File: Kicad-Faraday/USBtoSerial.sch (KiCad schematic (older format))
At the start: 10 parts, among them P16 USB-MICRO-B, U10 NUF2101MT1G, U6 FT230XQ-R

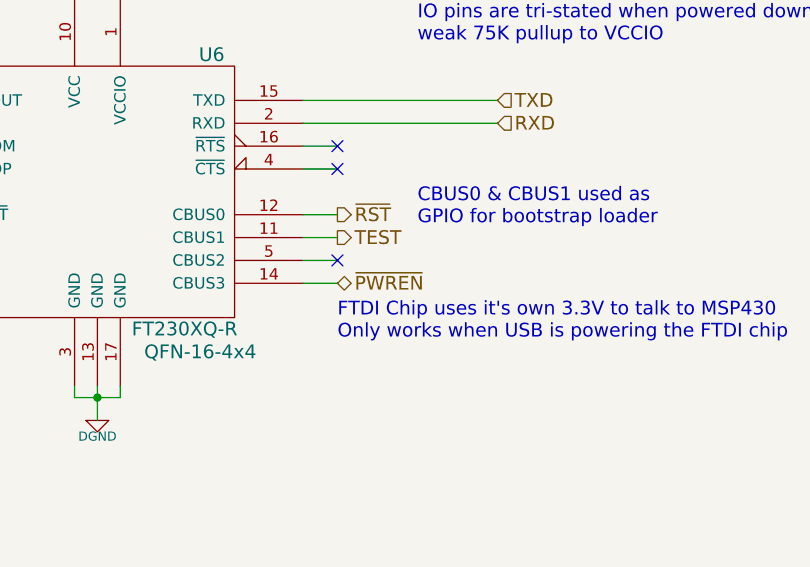
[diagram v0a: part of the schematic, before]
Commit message: Updated per RevD Github Issue comments. Largely removed unnecessary items
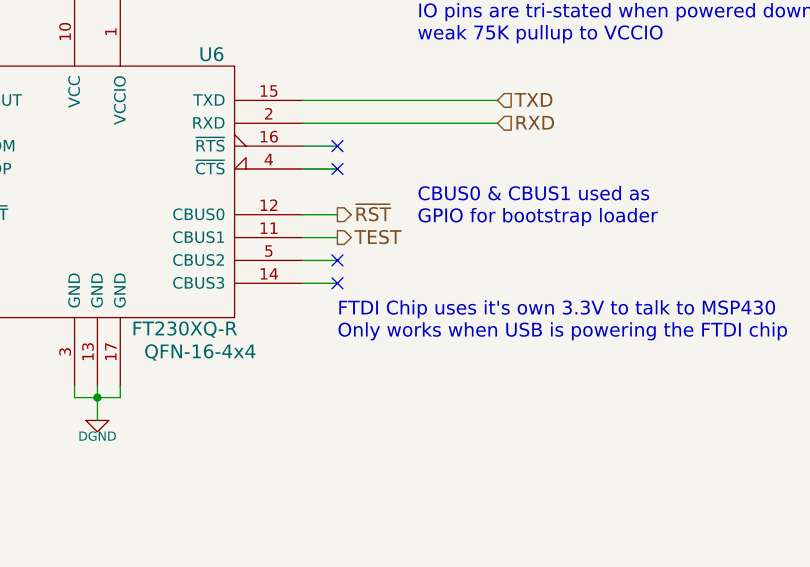
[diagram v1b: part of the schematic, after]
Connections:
- net ~PWREN~: no longer names the net of U6.14 (CBUS3)
- no-connect marks 4 -> 5
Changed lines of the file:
@@
 Sheet 8 11
 Title "Faraday Wireless Node"
-Date "24 oct 2016"
+Date "10 nov 2016"
 Rev "C"
 Comp "FaradayRF"
@@
 $EndComp
 $Comp
-L PWR_FLAG #FLG078
+L PWR_FLAG #FLG072
 U 1 1 54090954
 P 800 6000
-F 0 "#FLG078" H 800 6095 30  0001 C CNN
+F 0 "#FLG072" H 800 6095 30  0001 C CNN
 F 1 "PWR_FLAG" H 800 6180 30  0000 C CNN
 F 2 "" H 800 6000 60  0000 C CNN
@@
 5V USB
 $Comp
-L PWR_FLAG #FLG079
+L PWR_FLAG #FLG073
 U 1 1 54170CB7
 P 7000 4550
-F 0 "#FLG079" H 7000 4645 30  0001 C CNN
+F 0 "#FLG073" H 7000 4645 30  0001 C CNN
 F 1 "PWR_FLAG" H 7000 4730 30  0000 C CNN
 F 2 "" H 7000 4550 60  0000 C CNN
@@
 FTDI 3.3V OUT\nPower Flag
 $Comp
-L PWR_FLAG #FLG080
+L PWR_FLAG #FLG074
 U 1 1 541715EA
 P 5250 2650
-F 0 "#FLG080" H 5250 2745 30  0001 C CNN
+F 0 "#FLG074" H 5250 2745 30  0001 C CNN
 F 1 "PWR_FLAG" H 5250 2830 30  0000 C CNN
 F 2 "" H 5250 2650 60  0000 C CNN
@@
 $EndComp
 $Comp
-L DGND #PWR081
+L DGND #PWR075
 U 1 1 55A55E2C
 P 8350 6000
-F 0 "#PWR081" H 8350 6000 40  0001 C CNN
+F 0 "#PWR075" H 8350 6000 40  0001 C CNN
 F 1 "DGND" H 8350 5930 40  0000 C CNN
 F 2 "~" H 8350 6000 60  0000 C CNN
@@
 $EndComp
 $Comp
-L DGND #PWR082
+L DGND #PWR076
 U 1 1 55A55E8C
 P 7000 4250
-F 0 "#PWR082" H 7000 4250 40  0001 C CNN
+F 0 "#PWR076" H 7000 4250 40  0001 C CNN
 F 1 "DGND" H 7000 4180 40  0000 C CNN
 F 2 "~" H 7000 4250 60  0000 C CNN
@@
 $EndComp
 $Comp
-L DGND #PWR083
+L DGND #PWR077
 U 1 1 55A55E92
 P 7600 3300
-F 0 "#PWR083" H 7600 3300 40  0001 C CNN
+F 0 "#PWR077" H 7600 3300 40  0001 C CNN
 F 1 "DGND" H 7600 3230 40  0000 C CNN
 F 2 "~" H 7600 3300 60  0000 C CNN
@@
 $EndComp
 $Comp
-L DGND #PWR084
+L DGND #PWR078
 U 1 1 55A55E9E
 P 2100 6900
-F 0 "#PWR084" H 2100 6900 40  0001 C CNN
+F 0 "#PWR078" H 2100 6900 40  0001 C CNN
 F 1 "DGND" H 2100 6830 40  0000 C CNN
 F 2 "~" H 2100 6900 60  0000 C CNN
@@
 $EndComp
 $Comp
-L DGND #PWR085
+L DGND #PWR079
 U 1 1 55A55EA4
 P 1550 6900
-F 0 "#PWR085" H 1550 6900 40  0001 C CNN
+F 0 "#PWR079" H 1550 6900 40  0001 C CNN
 F 1 "DGND" H 1550 6830 40  0000 C CNN
 F 2 "~" H 1550 6900 60  0000 C CNN
@@
 $EndComp
 $Comp
-L +5V #PWR086
+L +5V #PWR080
 U 1 1 5788A803
 P 8250 2700
-F 0 "#PWR086" H 8250 2790 20  0001 C CNN
+F 0 "#PWR080" H 8250 2790 20  0001 C CNN
 F 1 "+5V" H 8250 2790 30  0000 C CNN
 F 2 "" H 8250 2700 60  0000 C CNN
@@
 	1    0    0    -1
 $EndComp
-Text HLabel 9400 5400 2    60   3State ~ 0
-~PWREN~
 $Comp
 L C C41
@@
 $EndComp
 $Comp
-L DGND #PWR087
+L DGND #PWR081
 U 1 1 578BD7EF
 P 5550 3300
-F 0 "#PWR087" H 5550 3300 40  0001 C CNN
+F 0 "#PWR081" H 5550 3300 40  0001 C CNN
 F 1 "DGND" H 5550 3230 40  0000 C CNN
 F 2 "~" H 5550 3300 60  0000 C CNN
@@
 $EndComp
 $Comp
-L DGND #PWR088
+L DGND #PWR082
 U 1 1 578CED94
 P 1100 6900
-F 0 "#PWR088" H 1100 6900 40  0001 C CNN
+F 0 "#PWR082" H 1100 6900 40  0001 C CNN
 F 1 "DGND" H 1100 6830 40  0000 C CNN
 F 2 "~" H 1100 6900 60  0000 C CNN
@@
 $EndComp
 $Comp
-L GNDPWR #PWR089
+L GNDPWR #PWR083
 U 1 1 578D0220
 P 800 6900
-F 0 "#PWR089" H 800 6950 40  0001 C CNN
+F 0 "#PWR083" H 800 6950 40  0001 C CNN
 F 1 "GNDPWR" H 800 6820 40  0000 C CNN
 F 2 "" H 800 6900 60  0000 C CNN
@@
 1Meg resistor for shield dischard\n4.7nF capacitor for RF noise
 $Comp
-L PWR_FLAG #FLG090
+L PWR_FLAG #FLG084
 U 1 1 578DEE25
 P 2300 6000
-F 0 "#FLG090" H 2300 6095 30  0001 C CNN
+F 0 "#FLG084" H 2300 6095 30  0001 C CNN
 F 1 "PWR_FLAG" H 2300 6180 30  0000 C CNN
 F 2 "" H 2300 6000 60  0000 C CNN
@@
 Wire Wire Line
 	9250 5300 9400 5300
-Wire Wire Line
-	9250 5400 9400 5400
 Wire Wire Line
 	5250 2650 5250 2700
@@
 IO pins are tri-stated when powered down,\nweak 75K pullup to VCCIO
 NoConn ~ 1950 5000
+NoConn ~ 9400 5400
+Wire Wire Line
+	9250 5400 9400 5400
 $EndSCHEMATC

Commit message: Adding Rev D files for night
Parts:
- C40: value 0.01uF -> 0.1uF
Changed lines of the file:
@@
 Sheet 8 11
 Title "Faraday Wireless Node"
-Date "13 nov 2016"
+Date "14 nov 2016"
 Rev "C"
 Comp "FaradayRF"
@@
 P 1100 6550
 F 0 "C40" H 1200 6600 50  0000 L CNN
-F 1 "0.01uF" H 1200 6525 50  0000 L CNN
+F 1 "0.1uF" H 1200 6525 50  0000 L CNN
 F 2 "C0402" H 1325 6375 50  0000 C CNN
 F 3 "" H 1100 6550 60  0000 C CNN

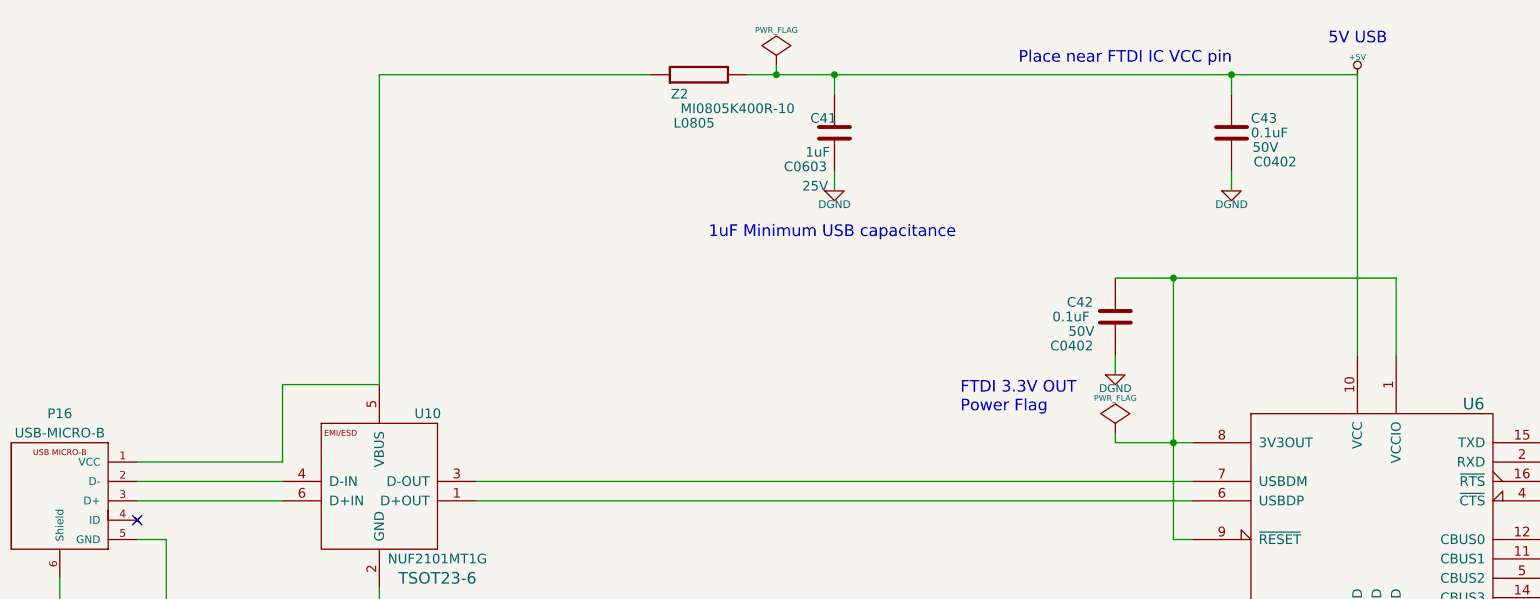
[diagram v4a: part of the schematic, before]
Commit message: Cleaned up a few connections on the schematic to make sure wire junctions were used. Also added a few notes such as LED color. Output new PDF of Schematics and updated Rev to Rev D1 for PCB:NG
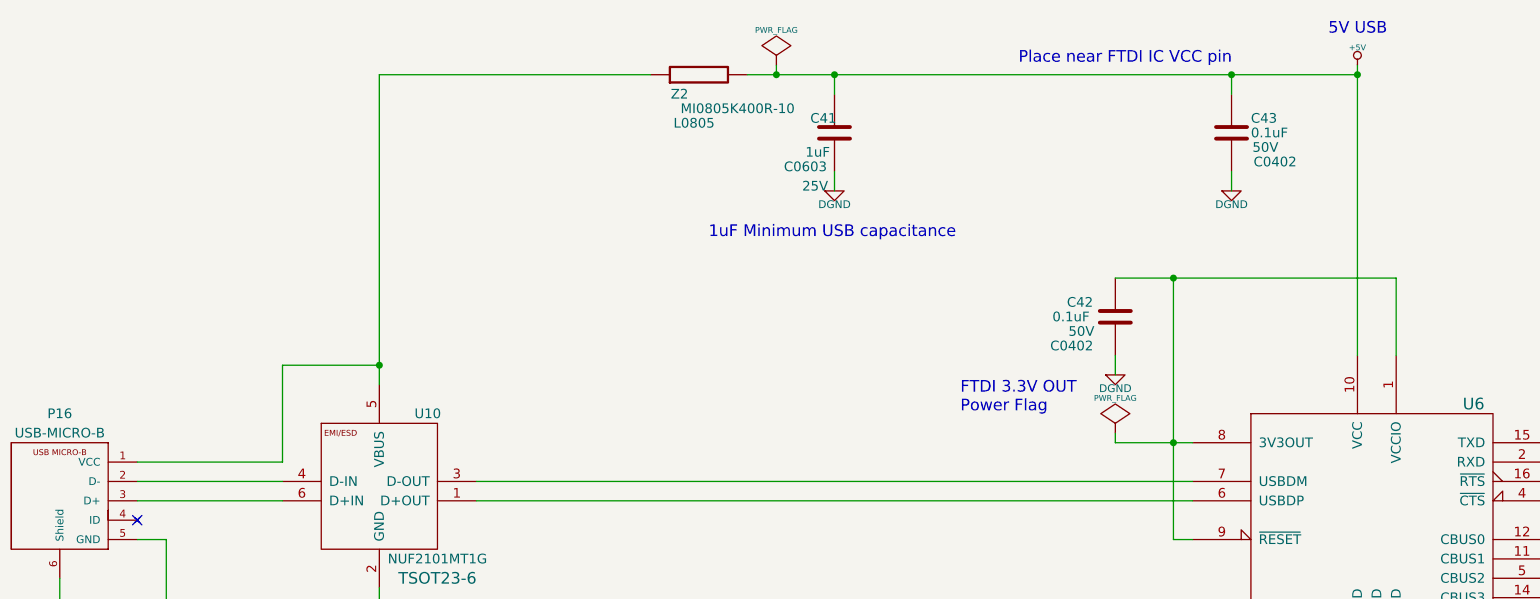
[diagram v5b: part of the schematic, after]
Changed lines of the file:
@@
 Sheet 8 11
 Title "Faraday Wireless Node"
-Date "14 nov 2016"
-Rev "C"
+Date "15 nov 2016"
+Rev "D1"
 Comp "FaradayRF"
 Comment1 "www.FaradayRF.com"
@@
 Text Notes 9400 5650 0    60   ~ 0
 FTDI Chip uses it's own 3.3V to talk to MSP430\nOnly works when USB is powering the FTDI chip
-Text Notes 8100 2550 0    60   ~ 0
+Text Notes 8100 2500 0    60   ~ 0
 5V USB
 $Comp
@@
 L +5V #PWR081
 U 1 1 5788A803
-P 8250 2700
-F 0 "#PWR081" H 8250 2790 20  0001 C CNN
-F 1 "+5V" H 8250 2790 30  0000 C CNN
-F 2 "" H 8250 2700 60  0000 C CNN
-F 3 "" H 8250 2700 60  0000 C CNN
-	1    8250 2700
+P 8250 2650
+F 0 "#PWR081" H 8250 2740 20  0001 C CNN
+F 1 "+5V" H 8250 2740 30  0000 C CNN
+F 2 "" H 8250 2650 60  0000 C CNN
+F 3 "" H 8250 2650 60  0000 C CNN
+	1    8250 2650
 	1    0    0    -1
 $EndComp
@@
 	3200 4300 3200 2700
 Wire Wire Line
-	2700 4300 3200 4300
-Wire Wire Line
-	2700 4700 2700 4300
-Wire Wire Line
-	1950 4700 2700 4700
+	2700 4200 2700 4700
+Wire Wire Line
+	2700 4700 1950 4700
 Wire Wire Line
 	1950 4900 2700 4900
@@
 	7600 3300 7600 3200
 Wire Wire Line
-	8250 2700 8250 4150
+	8250 2650 8250 4150
 Wire Wire Line
 	9250 4700 10100 4700
@@
 Wire Wire Line
 	9250 5400 9400 5400
+Wire Wire Line
+	2700 4200 3200 4200
+Connection ~ 3200 4200
+Connection ~ 8250 2700
 $EndSCHEMATC
